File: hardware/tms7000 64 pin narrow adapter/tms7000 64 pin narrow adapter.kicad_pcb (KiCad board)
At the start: 2 copper layers, 40.5 x 52.1 mm, 4 parts, among them J1 plcc 68, U1 DIP40 male pins

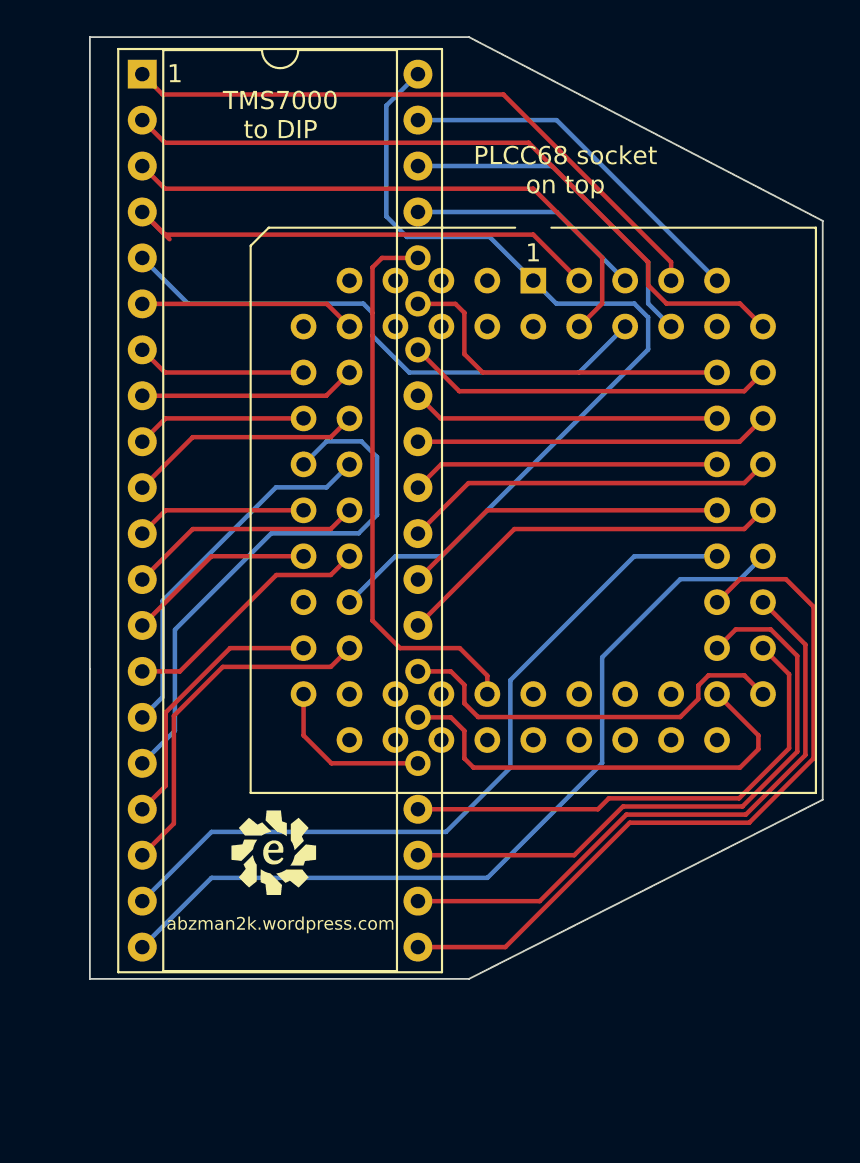
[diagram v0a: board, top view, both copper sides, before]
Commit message: fixed plcc88, added qfp60, dip54, dip64, and dip64 small pitch
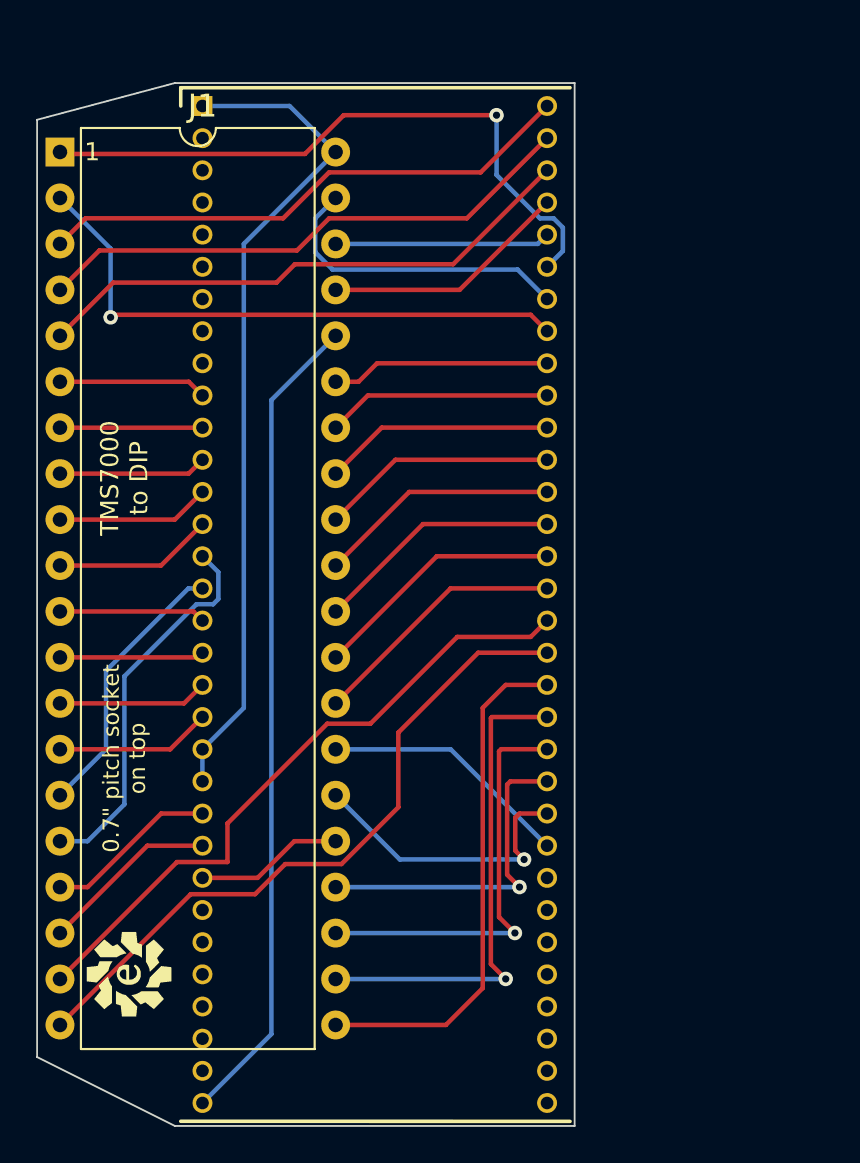
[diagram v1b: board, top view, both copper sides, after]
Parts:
- J1: value plcc 68 -> DIP64; footprint Package_LCC:PLCC-68_THT-Socket -> Evan's misc parts:DIP 64 1.78mm
- U1: footprint Package_DIP:DIP-40_W15.24mm_Socket -> Package_DIP:DIP-40_W15.24mm
- moved J1 20.7 mm to (123.4, 50.3)
- moved G*** 12.7 mm to (135.4, 100.8), turned to -90 degrees
- moved G*** 10.5 mm to (119.4, 98.3), turned to 90 degrees
- moved U1 6.26 mm to (115.6, 52.8)
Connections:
- J1 pad 10: F7 -> A0
- J1 pad 11: A0 -> A1
- J1 pad 12: A1 -> A2
- J1 pad 13: A2 -> A3
- J1 pad 14: A3 -> A4
- J1 pad 15: A4 -> A5
- J1 pad 16: A5 -> A6
- J1 pad 17: A6 -> A7
- J1 pad 18: A7 -> /INT3
- J1 pad 19: /INT3 -> /INT1
- J1 pad 20: /INT1 -> /RESET
- J1 pad 21: /RESET -> Vss
- J1 pad 22: /HALT -> Vss
- J1 pad 23: Vss -> XTAL2
- J1 pad 24: XTAL2 -> XTAL1
- J1 pad 25: XTAL1 -> Vcc
- J1 pad 26: Vcc -> G0
- J1 pad 27: G0 -> G1
- J1 pad 28: unconnected-(J1-Pad28) -> G2
- J1 pad 29: G1 -> G3
- J1 pad 30: G2 -> G4
- J1 pad 31: G3 -> G5
- J1 pad 32: G4 -> MC
- J1 pad 33: G5 -> E0
- J1 pad 34: MC -> E1
- J1 pad 35: E0 -> E2
- J1 pad 36: E1 -> E3
- J1 pad 37: E2 -> E4
- J1 pad 38: E3 -> E5
- J1 pad 39: E4 -> E6
- J1 pad 40: E5 -> E7
- J1 pad 41: E6 -> D0
- J1 pad 42: E7 -> D1
- J1 pad 43: unconnected-(J1-Pad43) -> D2
- J1 pad 44: D0 -> D3
- J1 pad 45: D1 -> D4
- J1 pad 46: D2 -> D5
- J1 pad 47: D3 -> D6
- J1 pad 48: D4 -> D7
- J1 pad 49: D5 -> C0
- J1 pad 50: D6 -> C1
- J1 pad 51: D7 -> C2
- J1 pad 52: C0 -> C3
- J1 pad 53: C1 -> C4
- J1 pad 54: C2 -> C5
- J1 pad 55: C3 -> C6
- J1 pad 56: C4 -> C7
- J1 pad 57: C5 -> B7
- J1 pad 58: C6 -> B6
- J1 pad 59: C7 -> B5
- J1 pad 60: B7 -> B4
- J1 pad 61: B6 -> B3
- J1 pad 62: unconnected-(J1-Pad62) -> B2
- J1 pad 63: B5 -> B1
- J1 pad 64: B4 -> B0
- J1 pad 9: unconnected-(J1-Pad9) -> F7
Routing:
- net MC: track 30.9 -> 45.5 mm
- net D5: track 41.1 -> 28.6 mm
- net D3: track 34.1 -> 23.0 mm, vias 0 -> 1
- net XTAL1: track 19.7 -> 9.88 mm
- net D2: track 28.1 -> 18.4 mm, vias 0 -> 1
- net D1: track 25.3 -> 16.3 mm, vias 0 -> 1
- net A5: track 30.1 -> 21.2 mm
- net D6: track 46.7 -> 37.9 mm
- net D0: track 22.5 -> 13.9 mm
- net C6: track 20.5 -> 12.4 mm
- net B7: track 39.8 -> 32.3 mm, vias 0 -> 1
- net C0: track 21.7 -> 14.3 mm
- net C7: track 19.4 -> 12.1 mm
- net B4: track 19.0 -> 11.9 mm
- net C2: track 20.7 -> 13.7 mm
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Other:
- board size 40.5 x 52.1 mm -> 29.7 x 57.7 mm
- board text added: "0.7{dblquote} pitch socket on top"
- board text removed: "PLCC68 socket on top"
